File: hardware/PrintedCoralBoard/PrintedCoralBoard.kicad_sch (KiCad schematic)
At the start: 14 parts, among them J1 DF40HC_3.0_-100DS-0.4V_51_, J2 DF40HC_3.0_-100DS-0.4V_51_, J4 Conn_02x25_Odd_Even, J5 Conn_02x25_Odd_Even, J6 Conn_02x25_Odd_Even, J7 Conn_02x25_Odd_Even

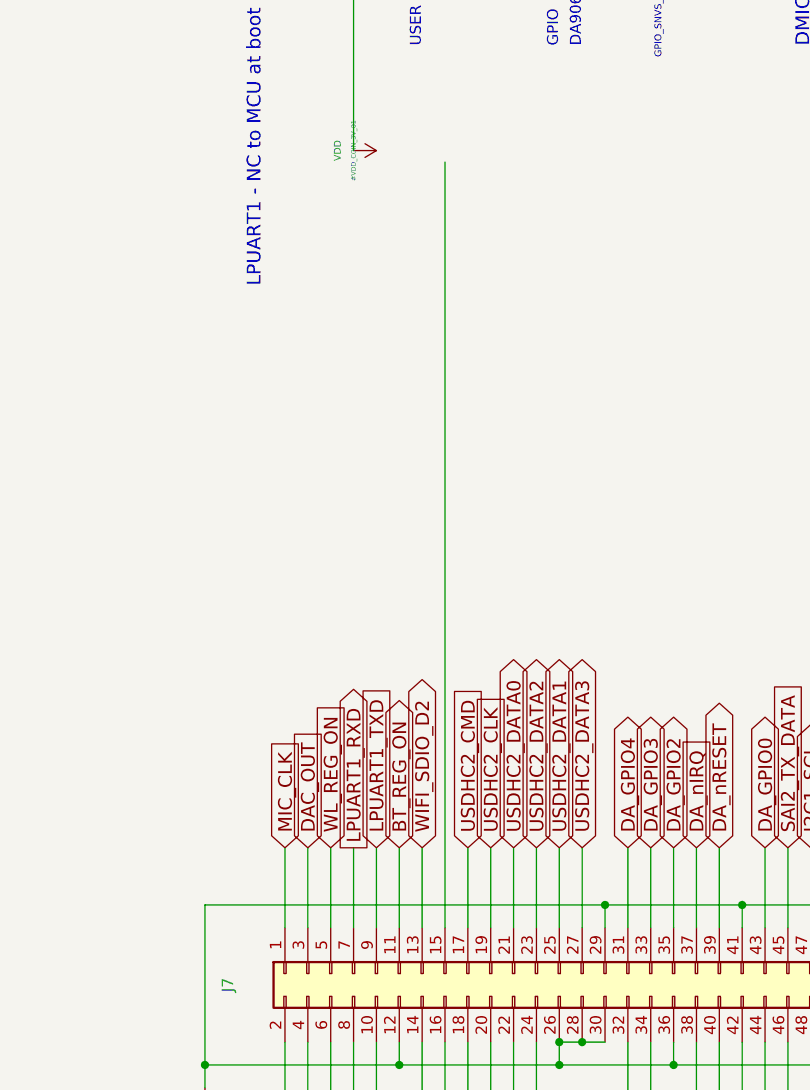
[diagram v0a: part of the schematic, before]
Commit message: fix landing pattern
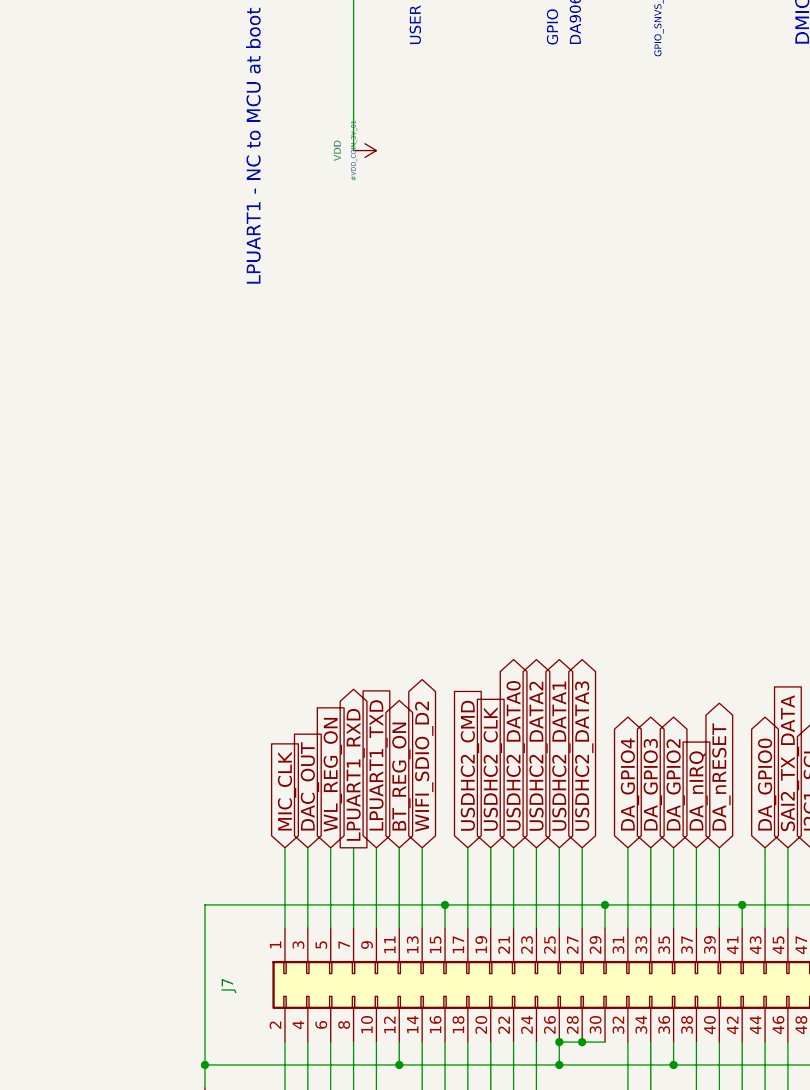
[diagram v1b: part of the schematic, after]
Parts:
- H1, H2, H3, H4: footprint MountingHole:MountingHole_2.7mm_M2.5_DIN965_Pad -> adcs:CoralLandingPad
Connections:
- net GND: now also J7.15 (Pin_15)

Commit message: add PiCoral 1.0.0
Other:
- moved on the sheet: J1
